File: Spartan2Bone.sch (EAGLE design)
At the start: 28 parts, among them IC01 XC2S30-5VQG100C100-VQFP-M, IC02 XCF01SVOG20C20-TSSOP-M, IC03 LM2937ET-3.3/NOPB

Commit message: Add labels.
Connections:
- net N$1 renamed REG33
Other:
- moved on the sheet: C6, C7, C8, C9, CN1, IC03, JTAG, MODE0, MODE1, MODE2, PCONF, POWER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

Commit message: Fixed ERC.
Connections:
- removed net VCCIO: C12.1, C4.1, C6.+, C8.1, CN1.19, CN1.29, CN1.9, IC01.I/O_VREF, IC01.I/O_VREF_10, IC01.I/O_VREF_11, IC01.I/O_VREF_12, IC01.I/O_VREF_13, IC01.I/O_VREF_14, IC01.I/O_VREF_15, IC01.I/O_VREF_16, IC01.VCCO, IC01.VCCO_6, IC01.VCCO_7, IC01.VCCO_8, IC03.IN, PCONF.1, POWER.2, SV2.11, SV2.17, SV2.5
- net VCCO: now also C12.1, C4.1, C6.+, C8.1, CN1.19, CN1.29, CN1.9, IC01.I/O_VREF, IC01.I/O_VREF_10, IC01.I/O_VREF_11, IC01.I/O_VREF_12, IC01.I/O_VREF_13, IC01.I/O_VREF_14, IC01.I/O_VREF_15, IC01.I/O_VREF_16, IC01.VCCO, IC01.VCCO_6, IC01.VCCO_7, IC01.VCCO_8, IC03.IN, PCONF.1, POWER.2, SV2.11, SV2.17, SV2.5
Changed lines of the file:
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@@
 <setting verticaltext="up"/>
 </settings>
-<grid distance="0.1" unitdist="inch" unit="inch" style="lines" multiple="1" display="yes" altdistance="0.01" altunitdist="inch" altunit="inch"/>
+<grid distance="0.1" unitdist="inch" unit="inch" style="lines" multiple="1" display="no" altdistance="0.01" altunitdist="inch" altunit="inch"/>
 <layers>
 <layer number="1" name="Top" color="4" fill="1" visible="no" active="no"/>
@@
 <part name="GND2" library="supply1" deviceset="GND" device=""/>
 <part name="GND3" library="supply1" deviceset="GND" device=""/>
-<part name="VCCO" library="supply1" deviceset="VCCIO" device="" value="VCCO"/>
-<part name="VCCO1" library="supply1" deviceset="VCCIO" device="" value="VCCO"/>
+<part name="VCCO" library="Spartan2Bone" deviceset="VCCO" device="" value="VCCO"/>
+<part name="VCCO1" library="Spartan2Bone" deviceset="VCCO" device="" value="VCCO"/>
 <part name="VCC1" library="supply1" deviceset="VCCINT" device=""/>
 <part name="VCC2" library="supply1" deviceset="VCCINT" device=""/>
@@
 <part name="R3" library="resistor" deviceset="R-US_" device="0204/5" value="4.7k"/>
 <part name="CN1" library="con-lsta" deviceset="FE17-2" device=""/>
-<part name="VCCO2" library="supply1" deviceset="VCCIO" device="" value="VCCO"/>
+<part name="VCCO2" library="Spartan2Bone" deviceset="VCCO" device="" value="VCCO"/>
 <part name="GND5" library="supply1" deviceset="GND" device=""/>
 <part name="SV2" library="con-lsta" deviceset="FE13-2" device=""/>
 <part name="POWER" library="jumper" deviceset="JP2E" device=""/>
-<part name="VCCO3" library="supply1" deviceset="VCCIO" device="" value="VCCO"/>
+<part name="VCCO3" library="Spartan2Bone" deviceset="VCCO" device="" value="VCCO"/>
 <part name="C6" library="resistor" deviceset="CPOL-US" device="E2.5-5" value="100uF"/>
 <part name="C7" library="resistor" deviceset="CPOL-US" device="E2.5-5" value="100uF"/>
@@
 <net name="VCCO" class="0">
 <segment>
-<pinref part="IC01" gate="A" pin="VCCO_5"/>
-<wire x1="289.56" y1="83.82" x2="256.54" y2="83.82" width="0.1524" layer="91"/>
-<wire x1="256.54" y1="83.82" x2="256.54" y2="96.52" width="0.1524" layer="91"/>
-<pinref part="VCCO" gate="G$1" pin="VCCIO"/>
-<pinref part="IC01" gate="A" pin="VCCO_4"/>
-<wire x1="256.54" y1="96.52" x2="256.54" y2="106.68" width="0.1524" layer="91"/>
-<wire x1="256.54" y1="106.68" x2="256.54" y2="116.84" width="0.1524" layer="91"/>
-<wire x1="256.54" y1="116.84" x2="256.54" y2="124.46" width="0.1524" layer="91"/>
-<wire x1="256.54" y1="124.46" x2="256.54" y2="134.62" width="0.1524" layer="91"/>
-<wire x1="256.54" y1="134.62" x2="256.54" y2="144.78" width="0.1524" layer="91"/>
-<wire x1="256.54" y1="144.78" x2="256.54" y2="160.02" width="0.1524" layer="91"/>
-<wire x1="256.54" y1="160.02" x2="256.54" y2="170.18" width="0.1524" layer="91"/>
-<wire x1="256.54" y1="170.18" x2="256.54" y2="180.34" width="0.1524" layer="91"/>
-<wire x1="256.54" y1="180.34" x2="256.54" y2="190.5" width="0.1524" layer="91"/>
-<wire x1="256.54" y1="190.5" x2="256.54" y2="200.66" width="0.1524" layer="91"/>
-<wire x1="256.54" y1="200.66" x2="256.54" y2="284.48" width="0.1524" layer="91"/>
-<wire x1="256.54" y1="116.84" x2="289.56" y2="116.84" width="0.1524" layer="91"/>
-<junction x="256.54" y="116.84"/>
-<pinref part="IC01" gate="A" pin="VCCO_3"/>
-<wire x1="256.54" y1="144.78" x2="289.56" y2="144.78" width="0.1524" layer="91"/>
-<junction x="256.54" y="144.78"/>
-<pinref part="IC01" gate="A" pin="VCCO_2"/>
-<wire x1="256.54" y1="180.34" x2="289.56" y2="180.34" width="0.1524" layer="91"/>
-<junction x="256.54" y="180.34"/>
-<pinref part="C2" gate="G$1" pin="1"/>
-<wire x1="256.54" y1="83.82" x2="256.54" y2="71.12" width="0.1524" layer="91"/>
-<junction x="256.54" y="83.82"/>
-<pinref part="IC01" gate="A" pin="I/O_VREF_2"/>
-<wire x1="256.54" y1="71.12" x2="256.54" y2="66.04" width="0.1524" layer="91"/>
-<wire x1="256.54" y1="200.66" x2="289.56" y2="200.66" width="0.1524" layer="91"/>
-<junction x="256.54" y="200.66"/>
-<pinref part="IC01" gate="A" pin="I/O_VREF_3"/>
-<wire x1="256.54" y1="190.5" x2="289.56" y2="190.5" width="0.1524" layer="91"/>
-<junction x="256.54" y="190.5"/>
-<pinref part="IC01" gate="A" pin="I/O_VREF_4"/>
-<wire x1="289.56" y1="170.18" x2="256.54" y2="170.18" width="0.1524" layer="91"/>
-<junction x="256.54" y="170.18"/>
-<pinref part="IC01" gate="A" pin="I/O_VREF_5"/>
-<wire x1="289.56" y1="160.02" x2="256.54" y2="160.02" width="0.1524" layer="91"/>
-<junction x="256.54" y="160.02"/>
-<pinref part="IC01" gate="A" pin="I/O_VREF_6"/>
-<wire x1="289.56" y1="134.62" x2="256.54" y2="134.62" width="0.1524" layer="91"/>
-<junction x="256.54" y="134.62"/>
-<pinref part="IC01" gate="A" pin="I/O_VREF_7"/>
-<wire x1="289.56" y1="124.46" x2="256.54" y2="124.46" width="0.1524" layer="91"/>
-<junction x="256.54" y="124.46"/>
-<pinref part="IC01" gate="A" pin="I/O_VREF_8"/>
-<wire x1="289.56" y1="106.68" x2="256.54" y2="106.68" width="0.1524" layer="91"/>
-<junction x="256.54" y="106.68"/>
-<pinref part="IC01" gate="A" pin="I/O_VREF_9"/>
-<wire x1="289.56" y1="96.52" x2="256.54" y2="96.52" width="0.1524" layer="91"/>
-<junction x="256.54" y="96.52"/>
-<pinref part="C11" gate="G$1" pin="1"/>
-<wire x1="266.7" y1="66.04" x2="266.7" y2="71.12" width="0.1524" layer="91"/>
-<wire x1="266.7" y1="71.12" x2="256.54" y2="71.12" width="0.1524" layer="91"/>
-<junction x="256.54" y="71.12"/>
-</segment>
-</net>
-<net name="VCCIO" class="0">
-<segment>
 <pinref part="IC01" gate="A" pin="VCCO_7"/>
 <wire x1="337.82" y1="147.32" x2="370.84" y2="147.32" width="0.1524" layer="91"/>
-<pinref part="VCCO1" gate="G$1" pin="VCCIO"/>
+<pinref part="VCCO1" gate="G$1" pin="VCCO"/>
 <wire x1="370.84" y1="147.32" x2="370.84" y2="162.56" width="0.1524" layer="91"/>
 <pinref part="IC01" gate="A" pin="VCCO_8"/>
@@
 </segment>
 <segment>
-<pinref part="VCCO2" gate="G$1" pin="VCCIO"/>
+<pinref part="VCCO2" gate="G$1" pin="VCCO"/>
 <wire x1="93.98" y1="284.48" x2="93.98" y2="243.84" width="0.1524" layer="91"/>
 <pinref part="CN1" gate="G$1" pin="9"/>
@@
 </segment>
 <segment>
-<pinref part="VCCO3" gate="G$1" pin="VCCIO"/>
+<pinref part="VCCO3" gate="G$1" pin="VCCO"/>
 <pinref part="POWER" gate="1" pin="2"/>
 <wire x1="7.62" y1="284.48" x2="7.62" y2="259.08" width="0.1524" layer="91"/>
@@
 <label x="-10.16" y="259.08" size="1.778" layer="95"/>
 </segment>
-</net>
+<segment>
+<pinref part="IC01" gate="A" pin="VCCO_5"/>
+<wire x1="289.56" y1="83.82" x2="256.54" y2="83.82" width="0.1524" layer="91"/>
+<wire x1="256.54" y1="83.82" x2="256.54" y2="96.52" width="0.1524" layer="91"/>
+<pinref part="VCCO" gate="G$1" pin="VCCO"/>
+<pinref part="IC01" gate="A" pin="VCCO_4"/>
+<wire x1="256.54" y1="96.52" x2="256.54" y2="106.68" width="0.1524" layer="91"/>
+<wire x1="256.54" y1="106.68" x2="256.54" y2="116.84" width="0.1524" layer="91"/>
+<wire x1="256.54" y1="116.84" x2="256.54" y2="124.46" width="0.1524" layer="91"/>
+<wire x1="256.54" y1="124.46" x2="256.54" y2="134.62" width="0.1524" layer="91"/>
+<wire x1="256.54" y1="134.62" x2="256.54" y2="144.78" width="0.1524" layer="91"/>
+<wire x1="256.54" y1="144.78" x2="256.54" y2="160.02" width="0.1524" layer="91"/>
+<wire x1="256.54" y1="160.02" x2="256.54" y2="170.18" width="0.1524" layer="91"/>
+<wire x1="256.54" y1="170.18" x2="256.54" y2="180.34" width="0.1524" layer="91"/>
+<wire x1="256.54" y1="180.34" x2="256.54" y2="190.5" width="0.1524" layer="91"/>
+<wire x1="256.54" y1="190.5" x2="256.54" y2="200.66" width="0.1524" layer="91"/>
+<wire x1="256.54" y1="200.66" x2="256.54" y2="284.48" width="0.1524" layer="91"/>
+<wire x1="256.54" y1="116.84" x2="289.56" y2="116.84" width="0.1524" layer="91"/>
+<junction x="256.54" y="116.84"/>
+<pinref part="IC01" gate="A" pin="VCCO_3"/>
+<wire x1="256.54" y1="144.78" x2="289.56" y2="144.78" width="0.1524" layer="91"/>
+<junction x="256.54" y="144.78"/>
+<pinref part="IC01" gate="A" pin="VCCO_2"/>
+<wire x1="256.54" y1="180.34" x2="289.56" y2="180.34" width="0.1524" layer="91"/>
+<junction x="256.54" y="180.34"/>
+<pinref part="C2" gate="G$1" pin="1"/>
+<wire x1="256.54" y1="83.82" x2="256.54" y2="71.12" width="0.1524" layer="91"/>
+<junction x="256.54" y="83.82"/>
+<pinref part="IC01" gate="A" pin="I/O_VREF_2"/>
+<wire x1="256.54" y1="71.12" x2="256.54" y2="66.04" width="0.1524" layer="91"/>
+<wire x1="256.54" y1="200.66" x2="289.56" y2="200.66" width="0.1524" layer="91"/>
+<junction x="256.54" y="200.66"/>
+<pinref part="IC01" gate="A" pin="I/O_VREF_3"/>
+<wire x1="256.54" y1="190.5" x2="289.56" y2="190.5" width="0.1524" layer="91"/>
+<junction x="256.54" y="190.5"/>
+<pinref part="IC01" gate="A" pin="I/O_VREF_4"/>
+<wire x1="289.56" y1="170.18" x2="256.54" y2="170.18" width="0.1524" layer="91"/>
+<junction x="256.54" y="170.18"/>
+<pinref part="IC01" gate="A" pin="I/O_VREF_5"/>
+<wire x1="289.56" y1="160.02" x2="256.54" y2="160.02" width="0.1524" layer="91"/>
+<junction x="256.54" y="160.02"/>
+<pinref part="IC01" gate="A" pin="I/O_VREF_6"/>
+<wire x1="289.56" y1="134.62" x2="256.54" y2="134.62" width="0.1524" layer="91"/>
+<junction x="256.54" y="134.62"/>
+<pinref part="IC01" gate="A" pin="I/O_VREF_7"/>
+<wire x1="289.56" y1="124.46" x2="256.54" y2="124.46" width="0.1524" layer="91"/>
+<junction x="256.54" y="124.46"/>
+<pinref part="IC01" gate="A" pin="I/O_VREF_8"/>
+<wire x1="289.56" y1="106.68" x2="256.54" y2="106.68" width="0.1524" layer="91"/>
+<junction x="256.54" y="106.68"/>
+<pinref part="IC01" gate="A" pin="I/O_VREF_9"/>
+<wire x1="289.56" y1="96.52" x2="256.54" y2="96.52" width="0.1524" layer="91"/>
+<junction x="256.54" y="96.52"/>
+<pinref part="C11" gate="G$1" pin="1"/>
+<wire x1="266.7" y1="66.04" x2="266.7" y2="71.12" width="0.1524" layer="91"/>
+<wire x1="266.7" y1="71.12" x2="256.54" y2="71.12" width="0.1524" layer="91"/>
+<junction x="256.54" y="71.12"/>
+</segment>
+</net>

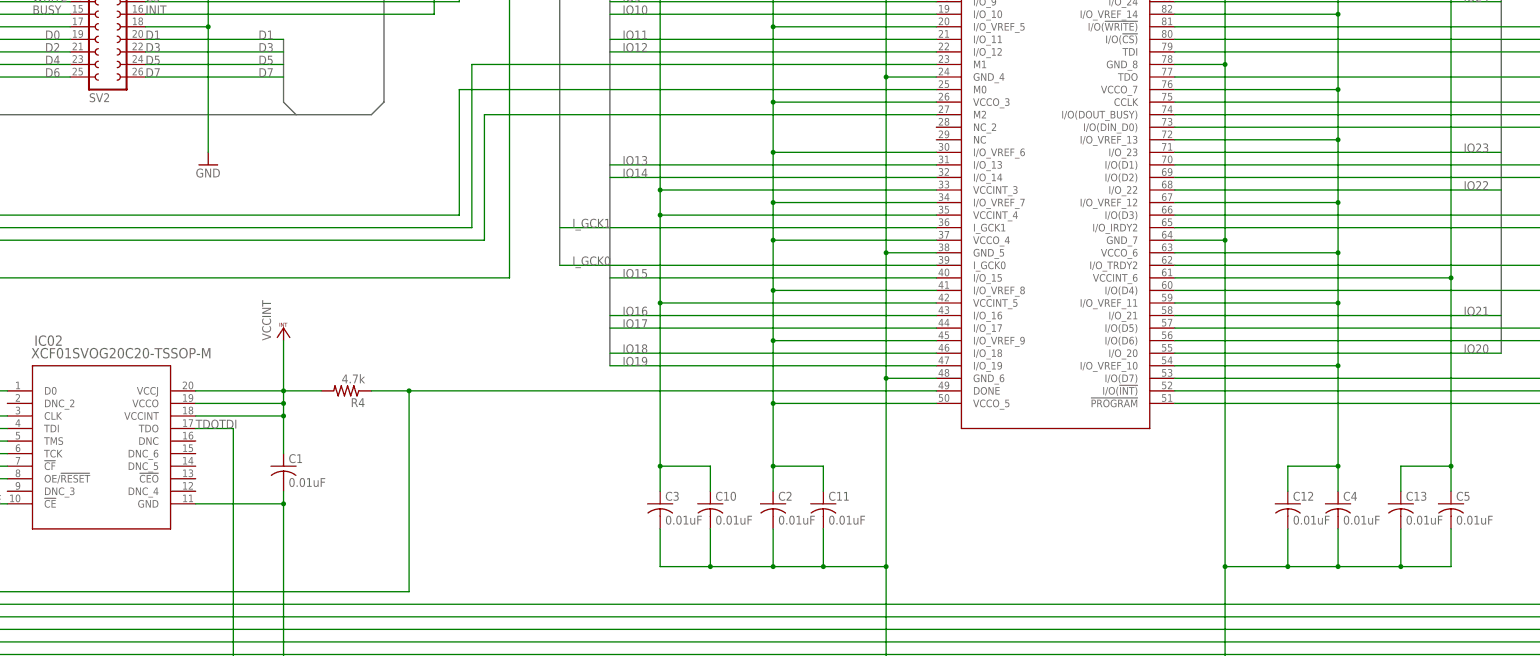
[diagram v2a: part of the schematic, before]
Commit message: Partial implement board design.
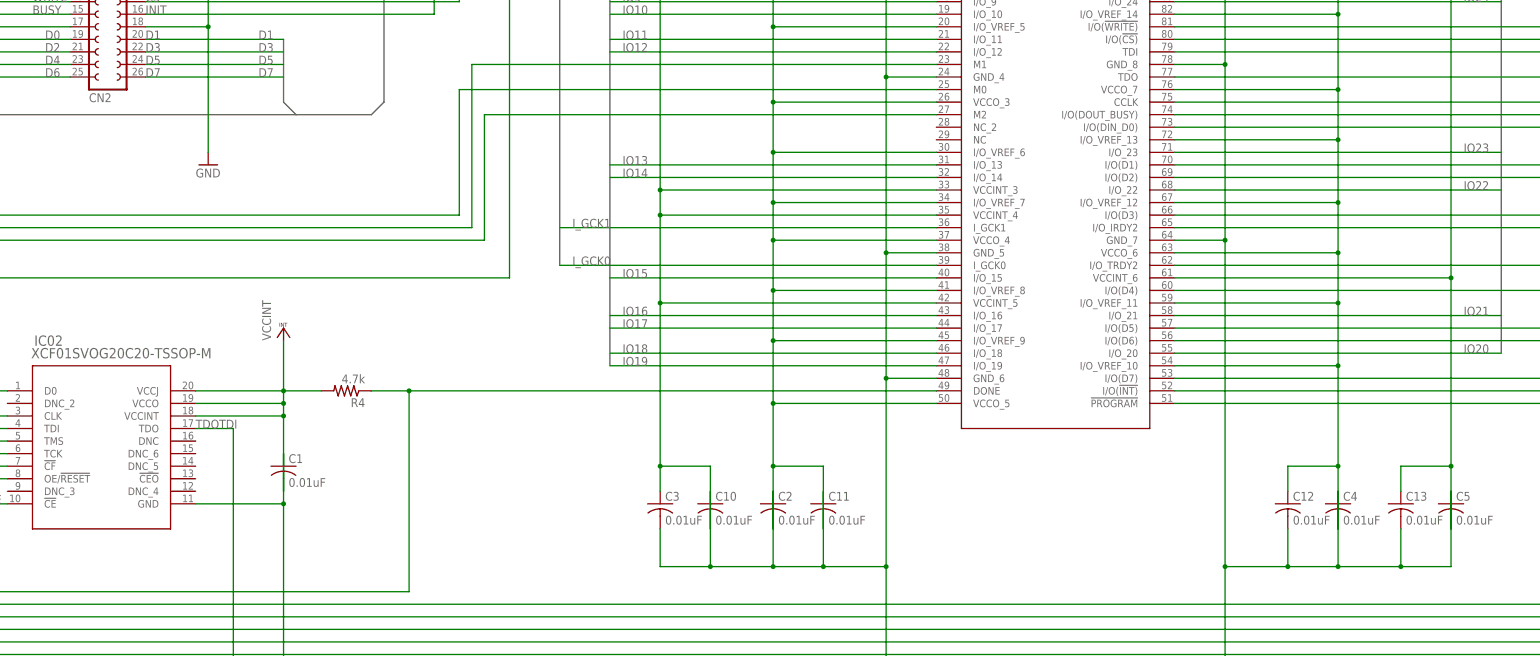
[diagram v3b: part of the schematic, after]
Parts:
- renumbered SV2 to CN2
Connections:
- net GND: now also C1.1, C10.1, C11.1, C2.1, C4.1, C5.1; no longer C1.2, C10.2, C11.2, C2.2, C4.2, C5.2
- net VCCINT: now also C1.2, C10.2, C5.2; no longer C1.1, C10.1, C5.1
- net VCCO: now also C11.2, C2.2, C4.2; no longer C11.1, C2.1, C4.1

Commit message: Testing.
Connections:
- net DONE: now also R4.2; no longer R4.1
- net GND: now also C2.2, C8.1, C9.1; no longer C2.1, C8.2, C9.2
- net VCCINT: now also C9.2, R4.1; no longer C9.1, R4.2
- net VCCO: now also C2.1, C8.2; no longer C2.2, C8.1
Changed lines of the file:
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@@
 <pinref part="IC02" gate="A" pin="!CE"/>
 <wire x1="93.98" y1="63.5" x2="101.6" y2="63.5" width="0.1524" layer="91"/>
-<pinref part="R4" gate="G$1" pin="1"/>
-<wire x1="175.26" y1="86.36" x2="182.88" y2="86.36" width="0.1524" layer="91"/>
+<pinref part="R4" gate="G$1" pin="2"/>
+<wire x1="165.1" y1="86.36" x2="182.88" y2="86.36" width="0.1524" layer="91"/>
 <junction x="182.88" y="86.36"/>
 <label x="93.98" y="63.5" size="1.778" layer="95"/>
@@
 <wire x1="233.68" y1="50.8" x2="243.84" y2="50.8" width="0.1524" layer="91"/>
 <junction x="279.4" y="50.8"/>
-<pinref part="C2" gate="G$1" pin="1"/>
+<pinref part="C2" gate="G$1" pin="2"/>
 <wire x1="243.84" y1="50.8" x2="256.54" y2="50.8" width="0.1524" layer="91"/>
 <wire x1="256.54" y1="50.8" x2="266.7" y2="50.8" width="0.1524" layer="91"/>
 <wire x1="266.7" y1="50.8" x2="279.4" y2="50.8" width="0.1524" layer="91"/>
-<wire x1="256.54" y1="66.04" x2="256.54" y2="50.8" width="0.1524" layer="91"/>
+<wire x1="256.54" y1="58.42" x2="256.54" y2="50.8" width="0.1524" layer="91"/>
 <junction x="256.54" y="50.8"/>
 <pinref part="C10" gate="G$1" pin="1"/>
@@
 <wire x1="25.4" y1="200.66" x2="25.4" y2="195.58" width="0.1524" layer="91"/>
 <junction x="25.4" y="195.58"/>
-<pinref part="C8" gate="G$1" pin="2"/>
-<wire x1="48.26" y1="200.66" x2="48.26" y2="195.58" width="0.1524" layer="91"/>
+<pinref part="C8" gate="G$1" pin="1"/>
+<wire x1="48.26" y1="208.28" x2="48.26" y2="195.58" width="0.1524" layer="91"/>
 <wire x1="48.26" y1="195.58" x2="35.56" y2="195.58" width="0.1524" layer="91"/>
 <junction x="35.56" y="195.58"/>
-<pinref part="C9" gate="G$1" pin="2"/>
-<wire x1="58.42" y1="200.66" x2="58.42" y2="195.58" width="0.1524" layer="91"/>
+<pinref part="C9" gate="G$1" pin="1"/>
+<wire x1="58.42" y1="208.28" x2="58.42" y2="195.58" width="0.1524" layer="91"/>
 <wire x1="58.42" y1="195.58" x2="48.26" y2="195.58" width="0.1524" layer="91"/>
 <junction x="48.26" y="195.58"/>
@@
 <wire x1="25.4" y1="215.9" x2="48.26" y2="215.9" width="0.1524" layer="91"/>
 <junction x="25.4" y="215.9"/>
-<pinref part="C8" gate="G$1" pin="1"/>
-<wire x1="48.26" y1="215.9" x2="48.26" y2="208.28" width="0.1524" layer="91"/>
+<pinref part="C8" gate="G$1" pin="2"/>
+<wire x1="48.26" y1="215.9" x2="48.26" y2="200.66" width="0.1524" layer="91"/>
 <pinref part="IC03" gate="A" pin="IN"/>
 <wire x1="7.62" y1="236.22" x2="20.32" y2="236.22" width="0.1524" layer="91"/>
@@
 <wire x1="256.54" y1="180.34" x2="289.56" y2="180.34" width="0.1524" layer="91"/>
 <junction x="256.54" y="180.34"/>
-<pinref part="C2" gate="G$1" pin="2"/>
+<pinref part="C2" gate="G$1" pin="1"/>
 <wire x1="256.54" y1="83.82" x2="256.54" y2="71.12" width="0.1524" layer="91"/>
 <junction x="256.54" y="83.82"/>
 <pinref part="IC01" gate="A" pin="I/O_VREF_2"/>
-<wire x1="256.54" y1="71.12" x2="256.54" y2="58.42" width="0.1524" layer="91"/>
+<wire x1="256.54" y1="71.12" x2="256.54" y2="66.04" width="0.1524" layer="91"/>
 <wire x1="256.54" y1="200.66" x2="289.56" y2="200.66" width="0.1524" layer="91"/>
 <junction x="256.54" y="200.66"/>
@@
 <wire x1="157.48" y1="66.04" x2="157.48" y2="81.28" width="0.1524" layer="91"/>
 <junction x="157.48" y="81.28"/>
-<pinref part="R4" gate="G$1" pin="2"/>
-<wire x1="165.1" y1="86.36" x2="157.48" y2="86.36" width="0.1524" layer="91"/>
+<pinref part="R4" gate="G$1" pin="1"/>
+<wire x1="175.26" y1="86.36" x2="157.48" y2="86.36" width="0.1524" layer="91"/>
 </segment>
 <segment>
@@
 <junction x="35.56" y="218.44"/>
 <wire x1="35.56" y1="218.44" x2="58.42" y2="218.44" width="0.1524" layer="91"/>
-<pinref part="C9" gate="G$1" pin="1"/>
-<wire x1="58.42" y1="218.44" x2="58.42" y2="208.28" width="0.1524" layer="91"/>
+<pinref part="C9" gate="G$1" pin="2"/>
+<wire x1="58.42" y1="218.44" x2="58.42" y2="200.66" width="0.1524" layer="91"/>
 <pinref part="PCONF" gate="1" pin="2"/>
 <wire x1="15.24" y1="256.54" x2="-10.16" y2="256.54" width="0.1524" layer="91"/>

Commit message: Testing.
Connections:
- net GND: now also C3.1; no longer C3.2
- net VCCINT: now also C3.2; no longer C3.1
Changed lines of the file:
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@@
 <pinref part="IC01" gate="A" pin="GND_2"/>
 <wire x1="279.4" y1="208.28" x2="289.56" y2="208.28" width="0.1524" layer="91"/>
-<pinref part="C3" gate="G$1" pin="2"/>
-<wire x1="233.68" y1="58.42" x2="233.68" y2="50.8" width="0.1524" layer="91"/>
+<pinref part="C3" gate="G$1" pin="1"/>
+<wire x1="233.68" y1="66.04" x2="233.68" y2="50.8" width="0.1524" layer="91"/>
 <wire x1="233.68" y1="50.8" x2="243.84" y2="50.8" width="0.1524" layer="91"/>
 <junction x="279.4" y="50.8"/>
@@
 <pinref part="IC01" gate="A" pin="VCCINT_5"/>
 <wire x1="233.68" y1="104.14" x2="289.56" y2="104.14" width="0.1524" layer="91"/>
-<pinref part="C3" gate="G$1" pin="1"/>
+<pinref part="C3" gate="G$1" pin="2"/>
 <wire x1="233.68" y1="104.14" x2="233.68" y2="71.12" width="0.1524" layer="91"/>
 <junction x="233.68" y="104.14"/>
 <pinref part="C10" gate="G$1" pin="2"/>
-<wire x1="233.68" y1="71.12" x2="233.68" y2="66.04" width="0.1524" layer="91"/>
+<wire x1="233.68" y1="71.12" x2="233.68" y2="58.42" width="0.1524" layer="91"/>
 <wire x1="243.84" y1="58.42" x2="243.84" y2="71.12" width="0.1524" layer="91"/>
 <wire x1="243.84" y1="71.12" x2="233.68" y2="71.12" width="0.1524" layer="91"/>

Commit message: Fixed board design.
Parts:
- removed JTAG: (no value), con-lstb:MA06-1
- removed MODE0, MODE1, MODE2: (no value), jumper:JP1Q
- removed PCONF, POWER: (no value), jumper:JP2E
- added CN3: JTAG, con-lstb:MA06-1
- added CN4: POWER, jumper:JP2E
- added CN5: PCONF, jumper:JP2E
- added JP1: MODE0, jumper:JP1Q
- added JP2: MODE1, jumper:JP1Q
- added JP3: MODE2, jumper:JP1Q
- CN1: value (none) -> IO[1..28]
- CN2: value (none) -> GCK RDY CNT D[0..7]
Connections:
- net GND: now also C1.2, C10.2, C11.2, C3.2, C4.2, C5.2, C8.2, C9.2, CN3.6, CN4.3; no longer C1.1, C10.1, C11.1, C3.1, C4.1, C5.1, C8.1, C9.1, JTAG.6, POWER.3
- net M0: now also JP1.2; no longer MODE0.2
- net M1: now also JP2.2; no longer MODE1.2
- net M2: now also JP3.2; no longer MODE2.2
- net REG33: now also CN5.3; no longer PCONF.3
- net TCK: now also CN3.3; no longer JTAG.4
- net TDI: now also CN3.5; no longer JTAG.2
- net TDO: now also CN3.4; no longer JTAG.5
- net TMS: now also CN3.2; no longer JTAG.3
- net VCCINT: now also C1.1, C10.1, C3.1, C5.1, C9.1, CN3.1, CN4.1, CN5.2, JP1.1, JP2.1, JP3.1; no longer C1.2, C10.2, C3.2, C5.2, C9.2, JTAG.1, MODE0.1, MODE1.1, MODE2.1, PCONF.2, POWER.1
- net VCCO: now also C11.1, C4.1, C8.1, CN4.2, CN5.1; no longer C11.2, C4.2, C8.2, PCONF.1, POWER.2
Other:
- note added: "Spartan2Bone 1.0 CC BY-NC-SA https://github.com/kekyo/Spartan2Bone"
- moved on the sheet: C1, C10, C11, C12, C13, C2, C3, C4, C5, C6, C7, C8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
